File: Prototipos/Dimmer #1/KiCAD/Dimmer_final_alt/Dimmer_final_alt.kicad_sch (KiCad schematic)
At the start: 27 parts, among them J2 Conn_01x02, K1 SRD-05VDC-SL-C, Q1 BC548B, Q2 BT137, U1 MOC3021M, U2 EL817

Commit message: Añadir punto de prueba y actualizar valor de resistencia R1 a 33k
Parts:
- added REF_VcaN: TestPoint, TestPoint:TestPoint_Loop_D1.80mm_Drill1.0mm_Beaded, symbol Connector:TestPoint
- D3: value D_Small -> 1N4007
- R1: value 47k -> 33k
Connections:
- net 48Vca_N: now also REF_VcaN.1
- net UC_DOUT renamed uC_DOUT
- net UC_PHASE renamed uC_PHASE
- net UC_RELAY renamed uC_RELAY
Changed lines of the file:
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@@
 	)
 	(junction
+		(at 46.99 82.55)
+		(diameter 0)
+		(color 0 0 0 0)
+	)
+	(junction
 		(at 107.95 127)
 		(diameter 0)
@@
 	(wire
 		(pts
+			(xy 36.83 82.55) (xy 46.99 82.55)
+		)
+		(stroke
+			(width 0)
+			(type default)
+		)
+	)
+	(wire
+		(pts
 			(xy 128.27 72.39) (xy 127 72.39)
 		)
@@
 		)
 	)
-	(global_label "UC_DOUT"
+	(global_label "uC_DOUT"
 		(shape input)
 		(at 82.55 49.53 180)
@@
 		)
 		(property "Intersheetrefs" "${INTERSHEET_REFS}"
-			(at 71.0981 49.53 0)
+			(at 71.2796 49.53 0)
 			(effects
 				(font
@@
 		)
 	)
-	(global_label "UC_PHASE"
+	(global_label "uC_PHASE"
 		(shape output)
 		(at 143.51 119.38 0)
@@
 		)
 		(property "Intersheetrefs" "${INTERSHEET_REFS}"
-			(at 156.1109 119.38 0)
+			(at 155.9294 119.38 0)
 			(effects
 				(font
@@
 		)
 	)
-	(global_label "UC_RELAY"
+	(global_label "uC_RELAY"
 		(shape output)
 		(at 194.31 60.96 180)
@@
 		)
 		(property "Intersheetrefs" "${INTERSHEET_REFS}"
-			(at 182.1324 60.96 0)
+			(at 182.3139 60.96 0)
 			(effects
 				(font
@@
 		)
 	)
-	(global_label "UC_RELAY"
+	(global_label "uC_RELAY"
 		(shape input)
 		(at 53.34 119.38 180)
@@
 		)
 		(property "Intersheetrefs" "${INTERSHEET_REFS}"
-			(at 41.1624 119.38 0)
+			(at 41.3439 119.38 0)
 			(effects
 				(font
@@
 		)
 	)
-	(global_label "UC_PHASE"
+	(global_label "uC_PHASE"
 		(shape input)
 		(at 228.6 78.74 0)
@@
 		)
 		(property "Intersheetrefs" "${INTERSHEET_REFS}"
-			(at 241.2009 78.74 0)
+			(at 241.0194 78.74 0)
 			(effects
 				(font
@@
 		)
 	)
-	(global_label "UC_DOUT"
+	(global_label "uC_DOUT"
 		(shape output)
 		(at 228.6 76.2 0)
@@
 		)
 		(property "Intersheetrefs" "${INTERSHEET_REFS}"
-			(at 240.0519 76.2 0)
+			(at 239.8704 76.2 0)
 			(effects
 				(font
@@
 	)
 	(symbol
+		(lib_id "Connector:TestPoint")
+		(at 36.83 82.55 0)
+		(unit 1)
+		(exclude_from_sim no)
+		(in_bom yes)
+		(on_board yes)
+		(dnp no)
+		(property "Reference" "REF_VcaN"
+			(at 35.052 77.47 0)
+			(effects
+				(font
+					(size 1.27 1.27)
+				)
+				(justify left)
+			)
+		)
+		(property "Value" "TestPoint"
+			(at 30.48 79.502 0)
+			(effects
+				(font
+					(size 1.27 1.27)
+				)
+				(justify left)
+				(hide yes)
+			)
+		)
+		(property "Footprint" "TestPoint:TestPoint_Loop_D1.80mm_Drill1.0mm_Beaded"
+			(at 41.91 82.55 0)
+			(effects
+				(font
+					(size 1.27 1.27)
+				)
+				(hide yes)
+			)
+		)
+		(property "Datasheet" "~"
+			(at 41.91 82.55 0)
+			(effects
+				(font
+					(size 1.27 1.27)
+				)
+				(hide yes)
+			)
+		)
+		(property "Description" "test point"
+			(at 36.83 82.55 0)
+			(effects
+				(font
+					(size 1.27 1.27)
+				)
+				(hide yes)
+			)
+		)
+		(pin "1"
+		)
+		(instances
+			(project "Dimmer_final_alt"
+				(path "/7934e872-2b7f-4f8f-a0b6-741d97320597"
+					(reference "REF_VcaN")
+					(unit 1)
+				)
+			)
+		)
+	)
+	(symbol
 		(lib_id "Device:R_Small")
 		(at 57.15 119.38 90)
@@
 			)
 		)
-		(property "Value" "D_Small"
+		(property "Value" "1N4007"
 			(at 118.11 80.01 0)
 			(effects
@@
 			)
 		)
-		(property "Value" "47k"
+		(property "Value" "33k"
 			(at 56.642 53.086 0)
 			(effects

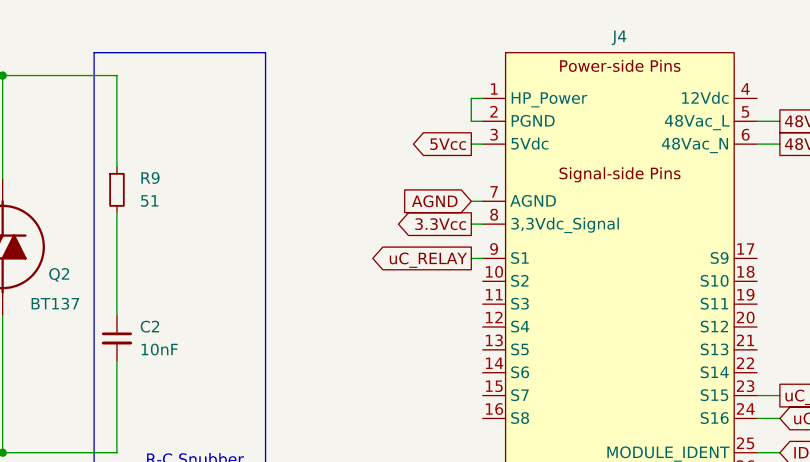
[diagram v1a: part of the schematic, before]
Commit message: Corregir HP_Power y PGND a AGND
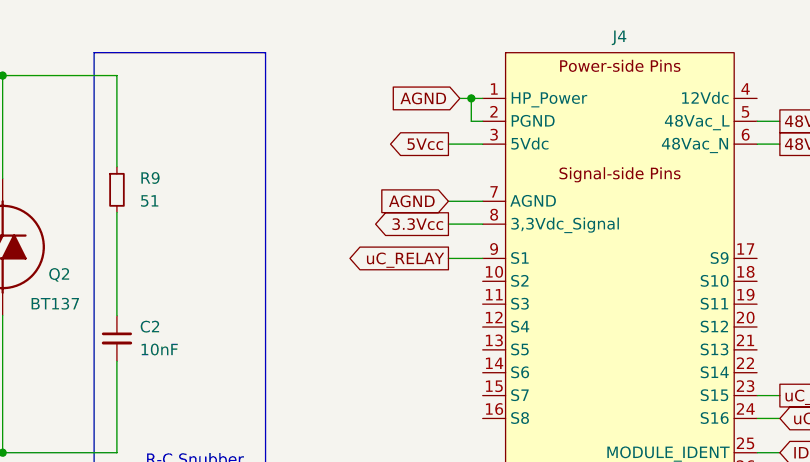
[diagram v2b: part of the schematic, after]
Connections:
- net AGND: now also J4.1 (HP_Power), J4.2 (PGND)
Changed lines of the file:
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@@
+	)
+	(junction
+		(at 194.31 43.18)
+		(diameter 0)
+		(color 0 0 0 0)
 	)
 	(junction
@@
 	(wire
 		(pts
-			(xy 195.58 45.72) (xy 194.31 45.72)
-		)
-		(stroke
-			(width 0)
-			(type default)
-		)
-	)
-	(wire
-		(pts
-			(xy 194.31 45.72) (xy 194.31 43.18)
-		)
-		(stroke
-			(width 0)
-			(type default)
-		)
-	)
-	(wire
-		(pts
 			(xy 45.72 52.07) (xy 46.99 52.07)
 		)
@@
 	(wire
 		(pts
+			(xy 194.31 45.72) (xy 195.58 45.72)
+		)
+		(stroke
+			(width 0)
+			(type default)
+		)
+	)
+	(wire
+		(pts
 			(xy 133.35 107.95) (xy 132.08 107.95)
 		)
@@
 	(wire
 		(pts
+			(xy 194.31 43.18) (xy 195.58 43.18)
+		)
+		(stroke
+			(width 0)
+			(type default)
+		)
+	)
+	(wire
+		(pts
 			(xy 63.5 46.99) (xy 63.5 48.26)
 		)
@@
 	(wire
 		(pts
-			(xy 195.58 54.61) (xy 194.31 54.61)
+			(xy 195.58 54.61) (xy 191.77 54.61)
 		)
 		(stroke
@@
 	(wire
 		(pts
-			(xy 194.31 48.26) (xy 195.58 48.26)
-		)
-		(stroke
-			(width 0)
-			(type default)
-		)
-	)
-	(wire
-		(pts
-			(xy 194.31 43.18) (xy 195.58 43.18)
+			(xy 191.77 48.26) (xy 195.58 48.26)
 		)
 		(stroke
@@
 	(wire
 		(pts
+			(xy 194.31 43.18) (xy 194.31 45.72)
+		)
+		(stroke
+			(width 0)
+			(type default)
+		)
+	)
+	(wire
+		(pts
 			(xy 107.95 127) (xy 107.95 124.46)
 		)
@@
 	(wire
 		(pts
-			(xy 195.58 57.15) (xy 194.31 57.15)
+			(xy 195.58 57.15) (xy 191.77 57.15)
 		)
 		(stroke
@@
 	(wire
 		(pts
+			(xy 193.04 43.18) (xy 194.31 43.18)
+		)
+		(stroke
+			(width 0)
+			(type default)
+		)
+	)
+	(wire
+		(pts
 			(xy 67.31 107.95) (xy 68.58 107.95)
 		)
@@
 	(wire
 		(pts
-			(xy 194.31 60.96) (xy 195.58 60.96)
+			(xy 191.77 60.96) (xy 195.58 60.96)
 		)
 		(stroke
@@
 		)
 	)
+	(global_label "AGND"
+		(shape input)
+		(at 193.04 43.18 180)
+		(fields_autoplaced yes)
+		(effects
+			(font
+				(size 1.27 1.27)
+			)
+			(justify right)
+		)
+		(property "Intersheetrefs" "${INTERSHEET_REFS}"
+			(at 185.0957 43.18 0)
+			(effects
+				(font
+					(size 1.27 1.27)
+				)
+				(justify right)
+				(hide yes)
+			)
+		)
+	)
 	(global_label "48Vca_N"
 		(shape output)
@@
 	(global_label "3.3Vcc"
 		(shape output)
-		(at 194.31 57.15 180)
-		(fields_autoplaced yes)
-		(effects
-			(font
-				(size 1.27 1.27)
-			)
-			(justify right)
-		)
-		(property "Intersheetrefs" "${INTERSHEET_REFS}"
-			(at 185.0352 57.15 0)
+		(at 191.77 57.15 180)
+		(fields_autoplaced yes)
+		(effects
+			(font
+				(size 1.27 1.27)
+			)
+			(justify right)
+		)
+		(property "Intersheetrefs" "${INTERSHEET_REFS}"
+			(at 182.4952 57.15 0)
 			(effects
 				(font
@@
 	(global_label "AGND"
 		(shape input)
-		(at 194.31 54.61 180)
-		(fields_autoplaced yes)
-		(effects
-			(font
-				(size 1.27 1.27)
-			)
-			(justify right)
-		)
-		(property "Intersheetrefs" "${INTERSHEET_REFS}"
-			(at 186.3657 54.61 0)
+		(at 191.77 54.61 180)
+		(fields_autoplaced yes)
+		(effects
+			(font
+				(size 1.27 1.27)
+			)
+			(justify right)
+		)
+		(property "Intersheetrefs" "${INTERSHEET_REFS}"
+			(at 183.8257 54.61 0)
 			(effects
 				(font
@@
 	(global_label "uC_RELAY"
 		(shape output)
-		(at 194.31 60.96 180)
-		(fields_autoplaced yes)
-		(effects
-			(font
-				(size 1.27 1.27)
-			)
-			(justify right)
-		)
-		(property "Intersheetrefs" "${INTERSHEET_REFS}"
-			(at 182.3139 60.96 0)
+		(at 191.77 60.96 180)
+		(fields_autoplaced yes)
+		(effects
+			(font
+				(size 1.27 1.27)
+			)
+			(justify right)
+		)
+		(property "Intersheetrefs" "${INTERSHEET_REFS}"
+			(at 179.7739 60.96 0)
 			(effects
 				(font
@@
 	(global_label "5Vcc"
 		(shape output)
-		(at 194.31 48.26 180)
-		(fields_autoplaced yes)
-		(effects
-			(font
-				(size 1.27 1.27)
-			)
-			(justify right)
-		)
-		(property "Intersheetrefs" "${INTERSHEET_REFS}"
-			(at 186.8495 48.26 0)
-			(effects
-				(font
+		(at 191.77 48.26 180)
+		(fields_autoplaced yes)
+		(effects
+			(font
+				(size 1.27 1.27)
+			)
+			(justify right)
+		)
+		(property "Intersheetrefs" "${INTERSHEET_REFS}"
+			(at 184.3095 48.26 0)
+			(effects
+				(font

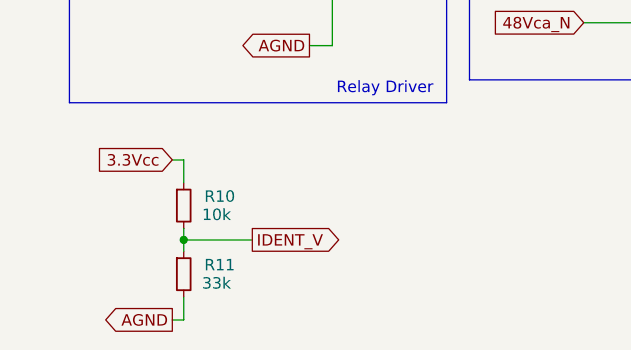
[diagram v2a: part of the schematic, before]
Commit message: Corregir esquemático de Dimmer
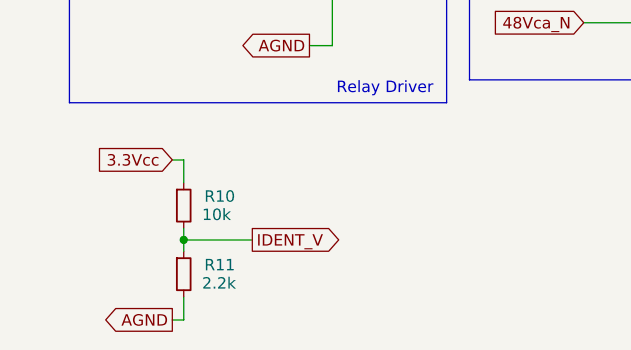
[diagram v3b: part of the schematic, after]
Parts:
- R11: value 33k -> 2.2k
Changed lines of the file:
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@@
 			)
 		)
-		(property "Value" "33k"
+		(property "Value" "2.2k"
 			(at 54.102 155.956 0)
 			(effects
